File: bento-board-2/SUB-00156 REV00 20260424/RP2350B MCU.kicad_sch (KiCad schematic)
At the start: 34 parts, among them J1 TC2030-MCP-NL, SW3 ${ALTIUM_VALUE}, SW4 ${ALTIUM_VALUE}, U1 ${ALTIUM_VALUE}, U2 ${ALTIUM_VALUE}, Y1 ${FREQUENCY}

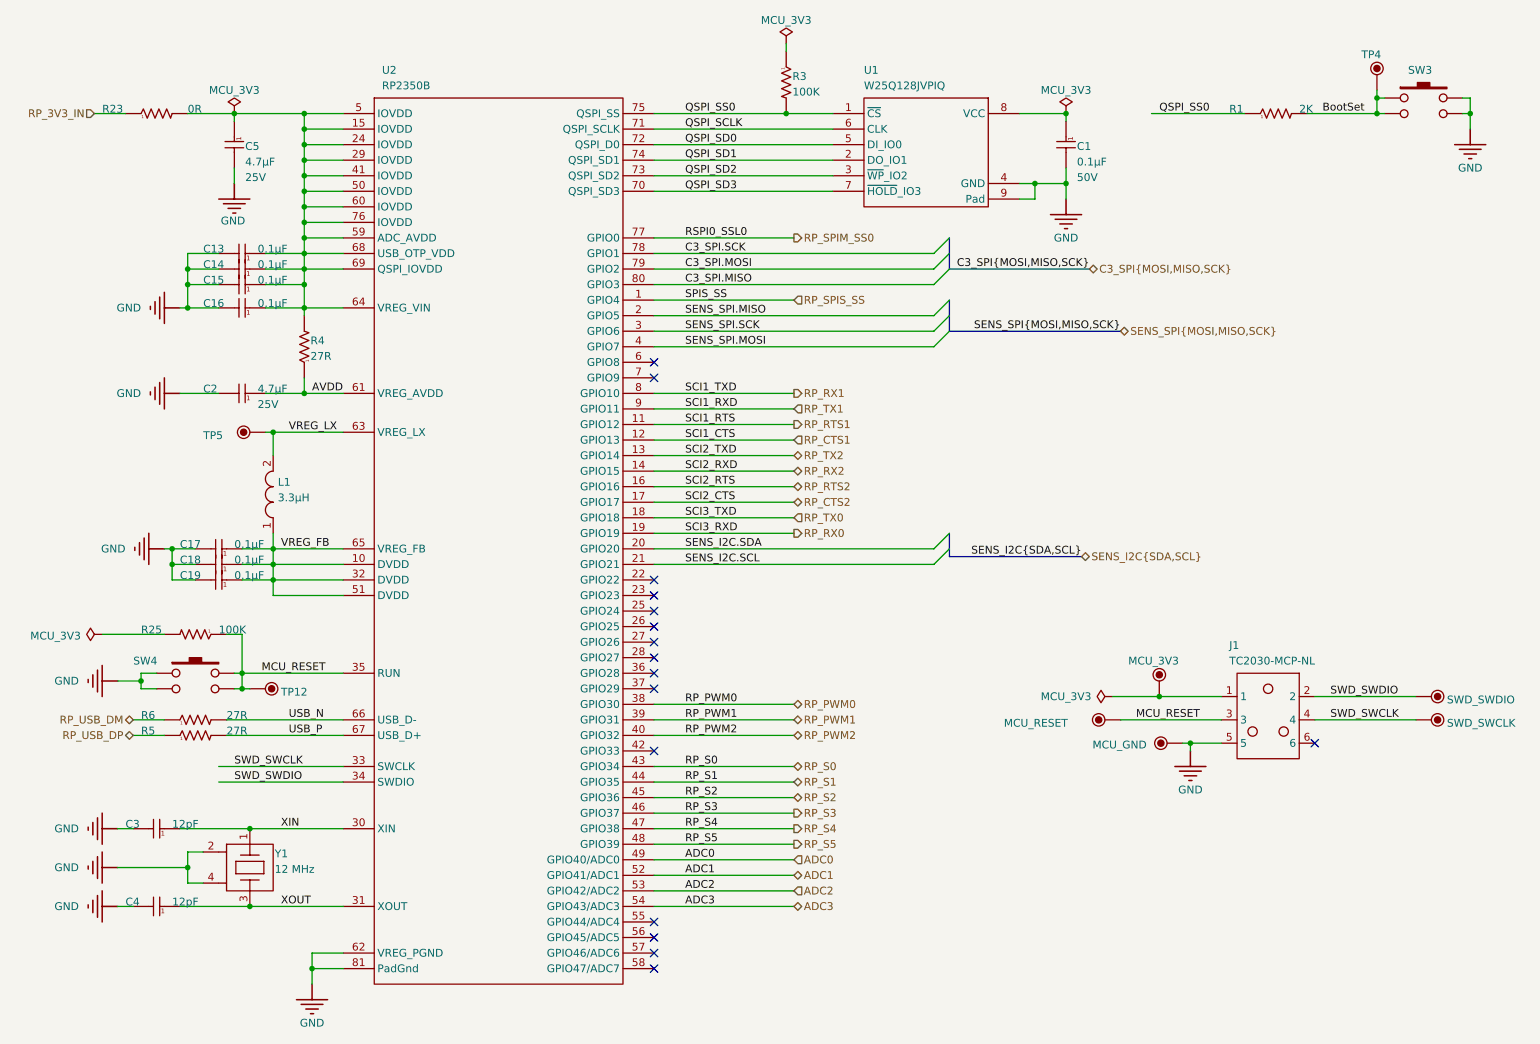
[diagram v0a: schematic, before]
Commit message: Add Bento Board 2 REV00 KiCad source files
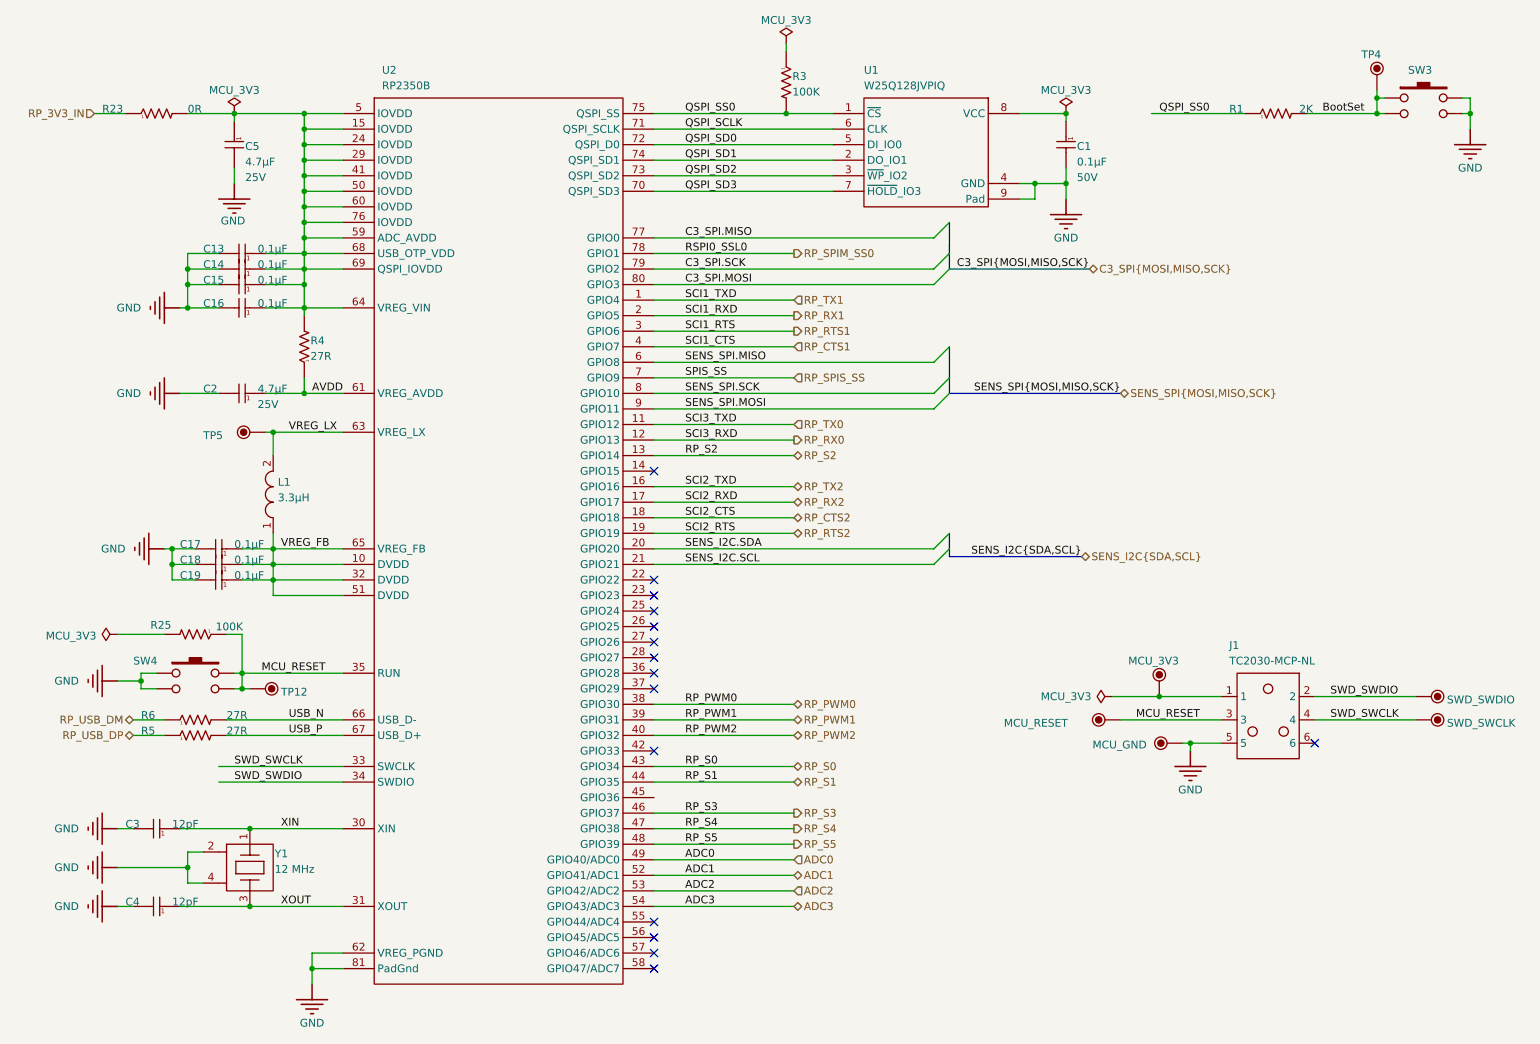
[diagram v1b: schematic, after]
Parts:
- removed R25: ${ALTIUM_VALUE}, Library:RC0603-N, symbol Library:root_2_RC0603FR-07100KL_BCDResistorCapacitorLibrary.IntLib
- added R25: ${ALTIUM_VALUE}, Library:RC0603-N, symbol Library:root_3_RC0603FR-07100KL_BCDResistorCapacitorLibrary.IntLib
- C1, C13, C14, C15, C16, C17, C18, C19, C2, C3, C4, C5, R1, R23, R3: FOOTPRINT 0603 (1608 Metric) -> (none)
- J1: footprint Library:TC2030-IDC -> (none)
- L1: footprint Library:IND-201610_SMD-2N -> (none)
- MCU_3V3, MCU_GND, MCU_RESET, SWD_SWCLK, SWD_SWDIO, TP12, TP4, TP5: footprint Library:TP-SM-39MILC -> (none)
- R4, R5, R6: FOOTPRINT R0603 -> (none)
- SW3, SW4: FOOTPRINT PTS810 -> (none)
- U1: FOOTPRINT 8-WSON (6x5) -> (none)
- U2: FOOTPRINT QFN-80-EP(10x10) -> (none)
- Y1: footprint Library:OSC3.2X2.5-4N -> (none)
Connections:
- net C3_SPI.MISO: now also U2.77 (GPIO0); no longer U2.80 (GPIO3)
- net C3_SPI.MOSI: now also U2.80 (GPIO3); no longer U2.79 (GPIO2)
- net C3_SPI.SCK: now also U2.79 (GPIO2); no longer U2.78 (GPIO1)
- net MCU_RESET: now also R25.1
- net RP_CTS1: now also U2.4 (GPIO7); no longer U2.12 (GPIO13)
- net RP_CTS2: now also U2.18 (GPIO18); no longer U2.17 (GPIO17)
- net RP_RTS1: now also U2.3 (GPIO6); no longer U2.11 (GPIO12)
- net RP_RTS2: now also U2.19 (GPIO19); no longer U2.16 (GPIO16)
- net RP_RX0: now also U2.12 (GPIO13); no longer U2.19 (GPIO19)
- net RP_RX1: now also U2.2 (GPIO5); no longer U2.8 (GPIO10)
- net RP_RX2: now also U2.17 (GPIO17); no longer U2.14 (GPIO15)
- net RP_S2: now also U2.13 (GPIO14); no longer U2.45 (GPIO36)
- net RP_SPIM_SS0: now also U2.78 (GPIO1); no longer U2.77 (GPIO0)
- net RP_SPIS_SS: now also U2.7 (GPIO9); no longer U2.1 (GPIO4)
- net RP_TX0: now also U2.11 (GPIO12); no longer U2.18 (GPIO18)
- net RP_TX1: now also U2.1 (GPIO4); no longer U2.9 (GPIO11)
- net RP_TX2: now also U2.16 (GPIO16); no longer U2.13 (GPIO14)
- net SENS_SPI.MISO: now also U2.6 (GPIO8); no longer U2.2 (GPIO5)
- net SENS_SPI.MOSI: now also U2.9 (GPIO11); no longer U2.4 (GPIO7)
- net SENS_SPI.SCK: now also U2.8 (GPIO10); no longer U2.3 (GPIO6)
- no-connect marks 16 -> 15
